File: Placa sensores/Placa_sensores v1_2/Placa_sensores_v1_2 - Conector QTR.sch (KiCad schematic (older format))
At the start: 15 parts, among them J1 Conn_02x08_Odd_Even, J10 Conn_01x01_Female, J11 Conn_01x01_Female, J12 Conn_01x01_Female, J13 Conn_01x01_Female, J2 Conn_01x01_Female, J3 Conn_01x01_Female, J4 Conn_01x01_Female, J5 Conn_01x01_Female, J6 Conn_01x01_Female, J7 Conn_01x01_Female, J8 Conn_01x01_Female, J9 Conn_01x01_Female

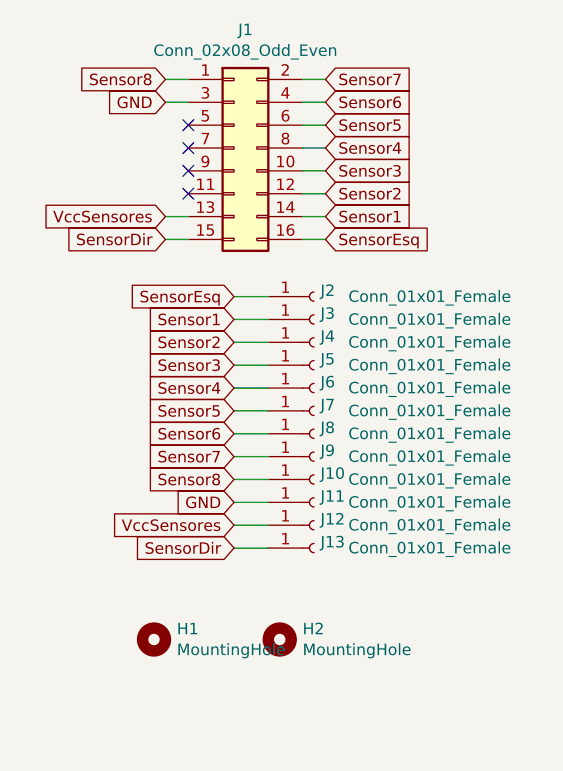
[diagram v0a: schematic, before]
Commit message: Acertada as placas e os pdfs
Acertada as placas centrais, de alimentação e de conector.
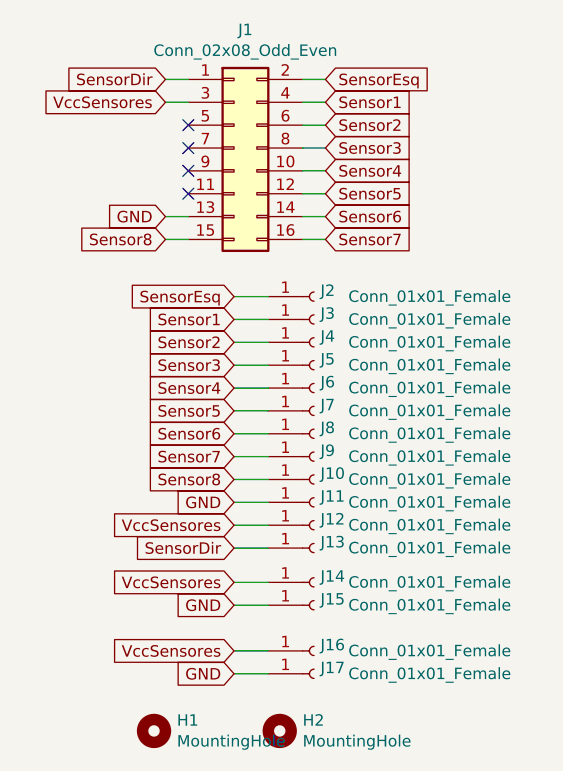
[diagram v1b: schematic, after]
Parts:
- added J14, J15, J16, J17: Conn_01x01_Female, Connector_PinSocket_2.54mm:PinSocket_1x01_P2.54mm_Vertical, symbol Connector:Conn_01x01_Female
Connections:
- net GND: now also J1.13 (Pin_13), J15.1 (Pin_1), J17.1 (Pin_1); no longer J1.3 (Pin_3)
- net Sensor1: now also J1.4 (Pin_4); no longer J1.14 (Pin_14)
- net Sensor2: now also J1.6 (Pin_6); no longer J1.12 (Pin_12)
- net Sensor3: now also J1.8 (Pin_8); no longer J1.10 (Pin_10)
- net Sensor4: now also J1.10 (Pin_10); no longer J1.8 (Pin_8)
- net Sensor5: now also J1.12 (Pin_12); no longer J1.6 (Pin_6)
- net Sensor6: now also J1.14 (Pin_14); no longer J1.4 (Pin_4)
- net Sensor7: now also J1.16 (Pin_16); no longer J1.2 (Pin_2)
- net Sensor8: now also J1.15 (Pin_15); no longer J1.1 (Pin_1)
- net SensorDir: now also J1.1 (Pin_1); no longer J1.15 (Pin_15)
- net SensorEsq: now also J1.2 (Pin_2); no longer J1.16 (Pin_16)
- net VccSensores: now also J1.3 (Pin_3), J14.1 (Pin_1), J16.1 (Pin_1); no longer J1.13 (Pin_13)
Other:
- moved on the sheet: H1, H2
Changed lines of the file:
@@
 $EndDescr
-$Comp
-L Connector_Generic:Conn_02x08_Odd_Even J1
-U 1 1 5D67E687
-P 1950 1850
-F 0 "J1" H 2000 2367 50  0000 C CNN
-F 1 "Conn_02x08_Odd_Even" H 2000 2276 50  0000 C CNN
-F 2 "Connector_IDC:IDC-Header_2x08_P2.54mm_Horizontal" H 1950 1850 50  0001 C CNN
-F 3 "~" H 1950 1850 50  0001 C CNN
-	1    1950 1850
-	1    0    0    -1
-$EndComp
-Text GLabel 1650 2250 0    50   Input ~ 0
-SensorDir
-Text GLabel 1650 1550 0    50   Input ~ 0
-Sensor8
-Text GLabel 1650 1650 0    50   Input ~ 0
-GND
-Text GLabel 1650 2150 0    50   Input ~ 0
-VccSensores
-Wire Wire Line
-	1650 1650 1750 1650
-Wire Wire Line
-	1650 1550 1750 1550
-Wire Wire Line
-	1650 2150 1750 2150
-Wire Wire Line
-	1650 2250 1750 2250
-Wire Wire Line
-	2250 2250 2350 2250
-Wire Wire Line
-	2250 2150 2350 2150
-Wire Wire Line
-	2250 2050 2350 2050
-Wire Wire Line
-	2250 1950 2350 1950
-Wire Wire Line
-	2250 1850 2350 1850
-Wire Wire Line
-	2350 1750 2250 1750
-Wire Wire Line
-	2250 1650 2350 1650
-Wire Wire Line
-	2250 1550 2350 1550
-NoConn ~ 1750 2050
-NoConn ~ 1750 1950
-NoConn ~ 1750 1850
-NoConn ~ 1750 1750
 $Comp
 L Connector:Conn_01x01_Female J2
@@
 	1    0    0    -1
 $EndComp
-Text GLabel 2350 1950 2    50   Input ~ 0
-Sensor3
-Text GLabel 2350 1550 2    50   Input ~ 0
-Sensor7
-Text GLabel 2350 1650 2    50   Input ~ 0
-Sensor6
-Text GLabel 2350 1750 2    50   Input ~ 0
-Sensor5
-Text GLabel 2350 1850 2    50   Input ~ 0
-Sensor4
-Text GLabel 2350 2050 2    50   Input ~ 0
-Sensor2
-Text GLabel 2350 2150 2    50   Input ~ 0
-Sensor1
-Text GLabel 2350 2250 2    50   Input ~ 0
-SensorEsq
 Text GLabel 1950 2800 0    50   Input ~ 0
 Sensor3
@@
 L Mechanical:MountingHole H1
 U 1 1 5D682DB8
-P 1600 4000
-F 0 "H1" H 1700 4046 50  0000 L CNN
-F 1 "MountingHole" H 1700 3955 50  0000 L CNN
-F 2 "MountingHole:MountingHole_3mm" H 1600 4000 50  0001 C CNN
-F 3 "~" H 1600 4000 50  0001 C CNN
-	1    1600 4000
+P 1600 4400
+F 0 "H1" H 1700 4446 50  0000 L CNN
+F 1 "MountingHole" H 1700 4355 50  0000 L CNN
+F 2 "MountingHole:MountingHole_3mm" H 1600 4400 50  0001 C CNN
+F 3 "~" H 1600 4400 50  0001 C CNN
+	1    1600 4400
 	1    0    0    -1
 $EndComp
@@
 L Mechanical:MountingHole H2
 U 1 1 5D6833E0
-P 2150 4000
-F 0 "H2" H 2250 4046 50  0000 L CNN
-F 1 "MountingHole" H 2250 3955 50  0000 L CNN
-F 2 "MountingHole:MountingHole_3mm" H 2150 4000 50  0001 C CNN
-F 3 "~" H 2150 4000 50  0001 C CNN
-	1    2150 4000
-	1    0    0    -1
-$EndComp
+P 2150 4400
+F 0 "H2" H 2250 4446 50  0000 L CNN
+F 1 "MountingHole" H 2250 4355 50  0000 L CNN
+F 2 "MountingHole:MountingHole_3mm" H 2150 4400 50  0001 C CNN
+F 3 "~" H 2150 4400 50  0001 C CNN
+	1    2150 4400
+	1    0    0    -1
+$EndComp
+$Comp
+L Connector:Conn_01x01_Female J17
+U 1 1 5D71832F
+P 2300 4150
+F 0 "J17" H 2328 4176 50  0000 L CNN
+F 1 "Conn_01x01_Female" H 2450 4150 50  0000 L CNN
+F 2 "Connector_PinSocket_2.54mm:PinSocket_1x01_P2.54mm_Vertical" H 2300 4150 50  0001 C CNN
+F 3 "~" H 2300 4150 50  0001 C CNN
+	1    2300 4150
+	1    0    0    -1
+$EndComp
+$Comp
+L Connector:Conn_01x01_Female J15
+U 1 1 5D719335
+P 2300 3850
+F 0 "J15" H 2328 3876 50  0000 L CNN
+F 1 "Conn_01x01_Female" H 2450 3850 50  0000 L CNN
+F 2 "Connector_PinSocket_2.54mm:PinSocket_1x01_P2.54mm_Vertical" H 2300 3850 50  0001 C CNN
+F 3 "~" H 2300 3850 50  0001 C CNN
+	1    2300 3850
+	1    0    0    -1
+$EndComp
+$Comp
+L Connector:Conn_01x01_Female J16
+U 1 1 5D719525
+P 2300 4050
+F 0 "J16" H 2328 4076 50  0000 L CNN
+F 1 "Conn_01x01_Female" H 2450 4050 50  0000 L CNN
+F 2 "Connector_PinSocket_2.54mm:PinSocket_1x01_P2.54mm_Vertical" H 2300 4050 50  0001 C CNN
+F 3 "~" H 2300 4050 50  0001 C CNN
+	1    2300 4050
+	1    0    0    -1
+$EndComp
+$Comp
+L Connector:Conn_01x01_Female J14
+U 1 1 5D71A00F
+P 2300 3750
+F 0 "J14" H 2328 3776 50  0000 L CNN
+F 1 "Conn_01x01_Female" H 2450 3750 50  0000 L CNN
+F 2 "Connector_PinSocket_2.54mm:PinSocket_1x01_P2.54mm_Vertical" H 2300 3750 50  0001 C CNN
+F 3 "~" H 2300 3750 50  0001 C CNN
+	1    2300 3750
+	1    0    0    -1
+$EndComp
+Text GLabel 1950 4150 0    50   Input ~ 0
+GND
+Text GLabel 1950 3850 0    50   Input ~ 0
+GND
+Text GLabel 1950 3750 0    50   Input ~ 0
+VccSensores
+Text GLabel 1950 4050 0    50   Input ~ 0
+VccSensores
+Wire Wire Line
+	1950 3750 2100 3750
+Wire Wire Line
+	2100 3850 1950 3850
+Wire Wire Line
+	1950 4050 2100 4050
+Wire Wire Line
+	2100 4150 1950 4150
+Text GLabel 1650 1550 0    50   Input ~ 0
+SensorDir
+Text GLabel 1650 2250 0    50   Input ~ 0
+Sensor8
+Text GLabel 1650 2150 0    50   Input ~ 0
+GND
+Text GLabel 2350 1850 2    50   Input ~ 0
+Sensor3
+Text GLabel 2350 2250 2    50   Input ~ 0
+Sensor7
+Text GLabel 2350 2150 2    50   Input ~ 0
+Sensor6
+Text GLabel 2350 2050 2    50   Input ~ 0
+Sensor5
+Text GLabel 2350 1950 2    50   Input ~ 0
+Sensor4
+Text GLabel 2350 1750 2    50   Input ~ 0
+Sensor2
+Text GLabel 2350 1650 2    50   Input ~ 0
+Sensor1
+Text GLabel 2350 1550 2    50   Input ~ 0
+SensorEsq
+NoConn ~ 1750 1750
+NoConn ~ 1750 1850
+NoConn ~ 1750 1950
+NoConn ~ 1750 2050
+Wire Wire Line
+	2250 1550 2350 1550
+Wire Wire Line
+	2250 1650 2350 1650
+Wire Wire Line
+	2350 1750 2250 1750
+Wire Wire Line
+	2250 1850 2350 1850
+Wire Wire Line
+	2250 1950 2350 1950
+Wire Wire Line
+	2250 2050 2350 2050
+Wire Wire Line
+	2250 2150 2350 2150
+Wire Wire Line
+	2250 2250 2350 2250
+Wire Wire Line
+	1650 2250 1750 2250
+Wire Wire Line
+	1650 2150 1750 2150
+Wire Wire Line
+	1650 1550 1750 1550
+Wire Wire Line
+	1650 1650 1750 1650
+$Comp
+L Connector_Generic:Conn_02x08_Odd_Even J1
+U 1 1 5D67E687
+P 1950 1850
+F 0 "J1" H 2000 2367 50  0000 C CNN
+F 1 "Conn_02x08_Odd_Even" H 2000 2276 50  0000 C CNN
+F 2 "Connector_IDC:IDC-Header_2x08_P2.54mm_Horizontal" H 1950 1850 50  0001 C CNN
+F 3 "~" H 1950 1850 50  0001 C CNN
+	1    1950 1850
+	1    0    0    -1
+$EndComp
+Text GLabel 1650 1650 0    50   Input ~ 0
+VccSensores
 $EndSCHEMATC
